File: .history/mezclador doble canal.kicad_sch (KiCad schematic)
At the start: 31 parts, among them J1 Conn_Coaxial, J2 Conn_Coaxial, J3 Conn_Coaxial, J4 Conn_Coaxial, J5 Conn_Coaxial, J6 Conn_Coaxial, J7 Screw_Terminal_01x02, U1 NE5532

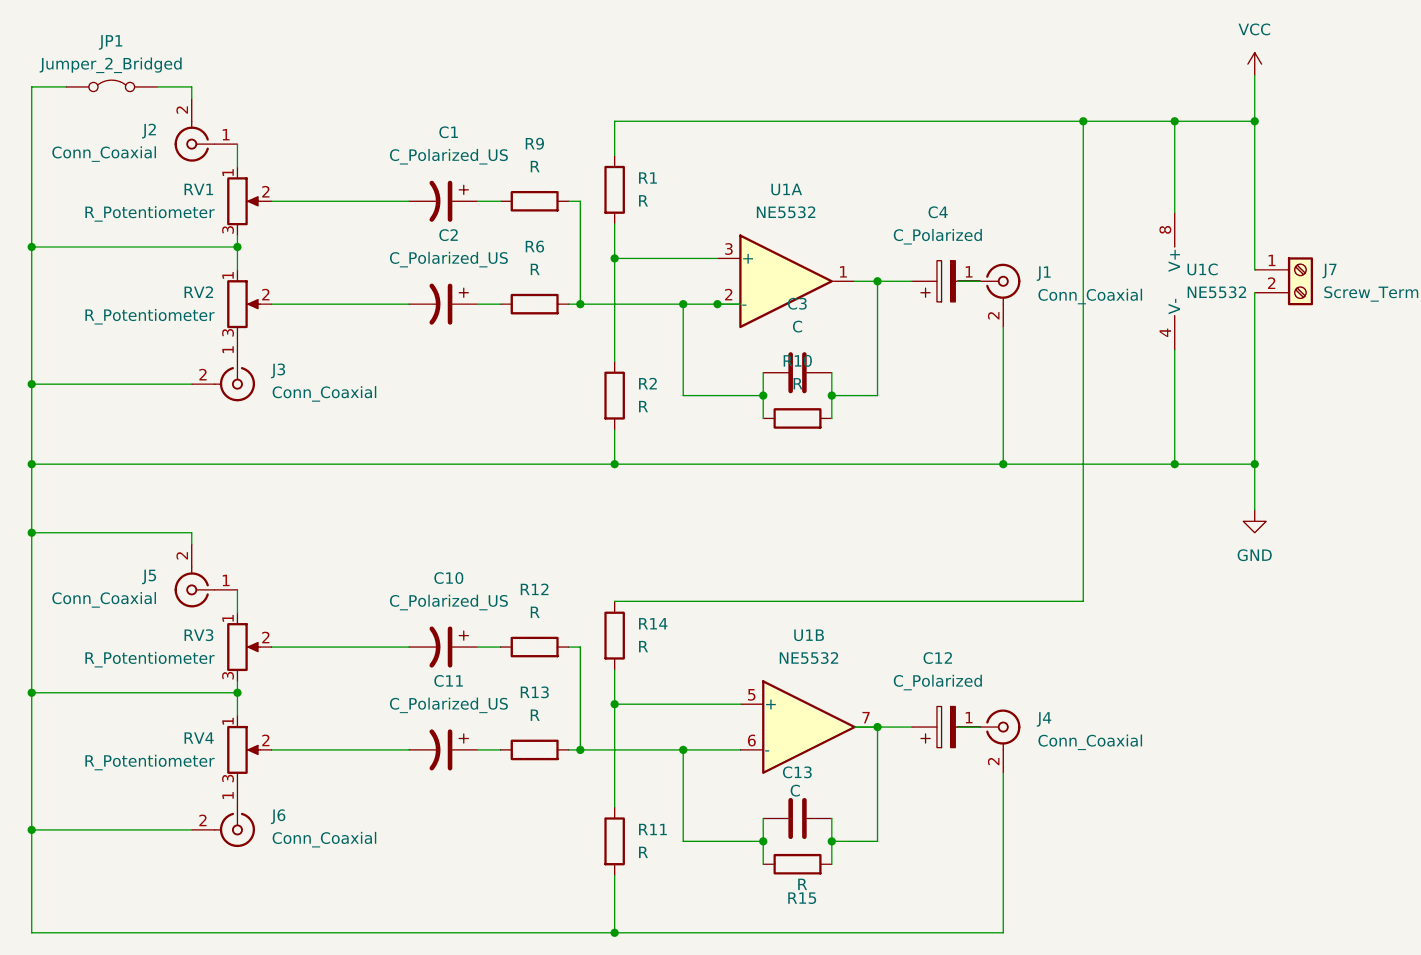
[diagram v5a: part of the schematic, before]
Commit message: mejorando distribucion de componentes
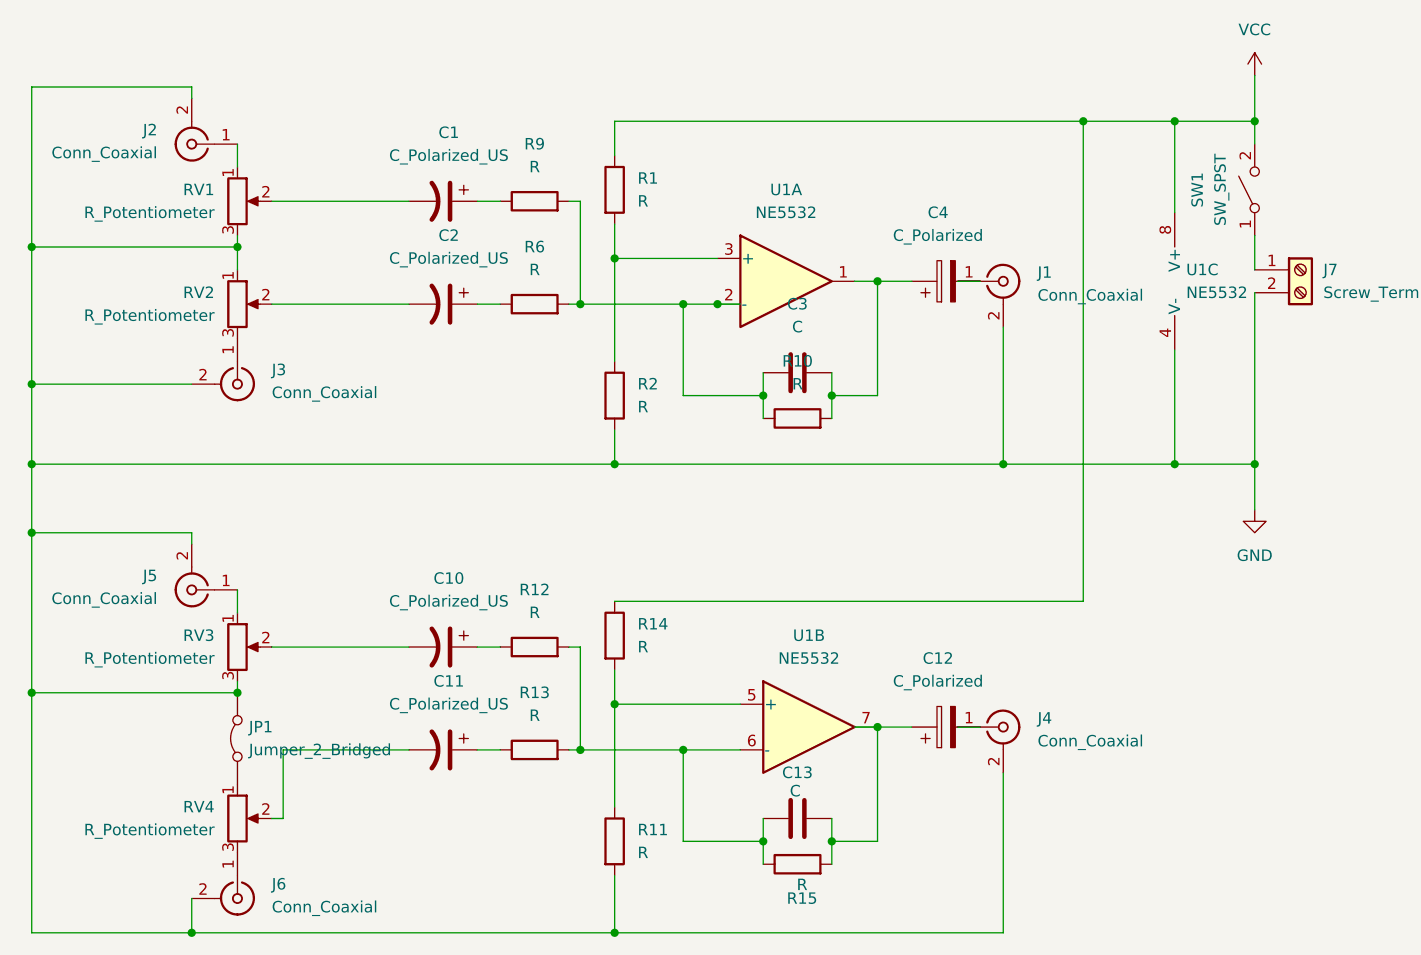
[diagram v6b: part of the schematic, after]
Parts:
- added SW1: SW_SPST, personal:double wire, symbol Switch:SW_SPST
- J4, J6: footprint Connector:JWT_A3963_1x02_P3.96mm_Vertical -> personal:double wire
- RV4: footprint Potentiometer_THT:Potentiometer_Bourns_3296W_Vertical -> personal:potentiometer pads
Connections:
- net GND: now also J2.2 (Ext), JP1.2 (B); no longer JP1.1 (A), RV4.1
- net VCC: now also SW1.2 (B); no longer J7.1 (Pin_1)
- new net: JP1.1 (A), RV4.1
- new net: J7.1 (Pin_1), SW1.1 (A)
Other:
- moved on the sheet: J6, RV4

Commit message: agregando preamplificador microfomo
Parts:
- added C5: C_Polarized_US, symbol Device:C_Polarized_US
- added J8: Conn_Coaxial, symbol Connector:Conn_Coaxial
- added R3: R, Package_LCC:PLCC-84_29.3x29.3mm_P1.27mm, symbol Device:R
- added U2: TL071, symbol Amplifier_Operational:TL071
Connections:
- new net: C5.2, J8.1 (In)
- new net: C5.1, R3.1
- new net: R3.2, U2.2 (-)

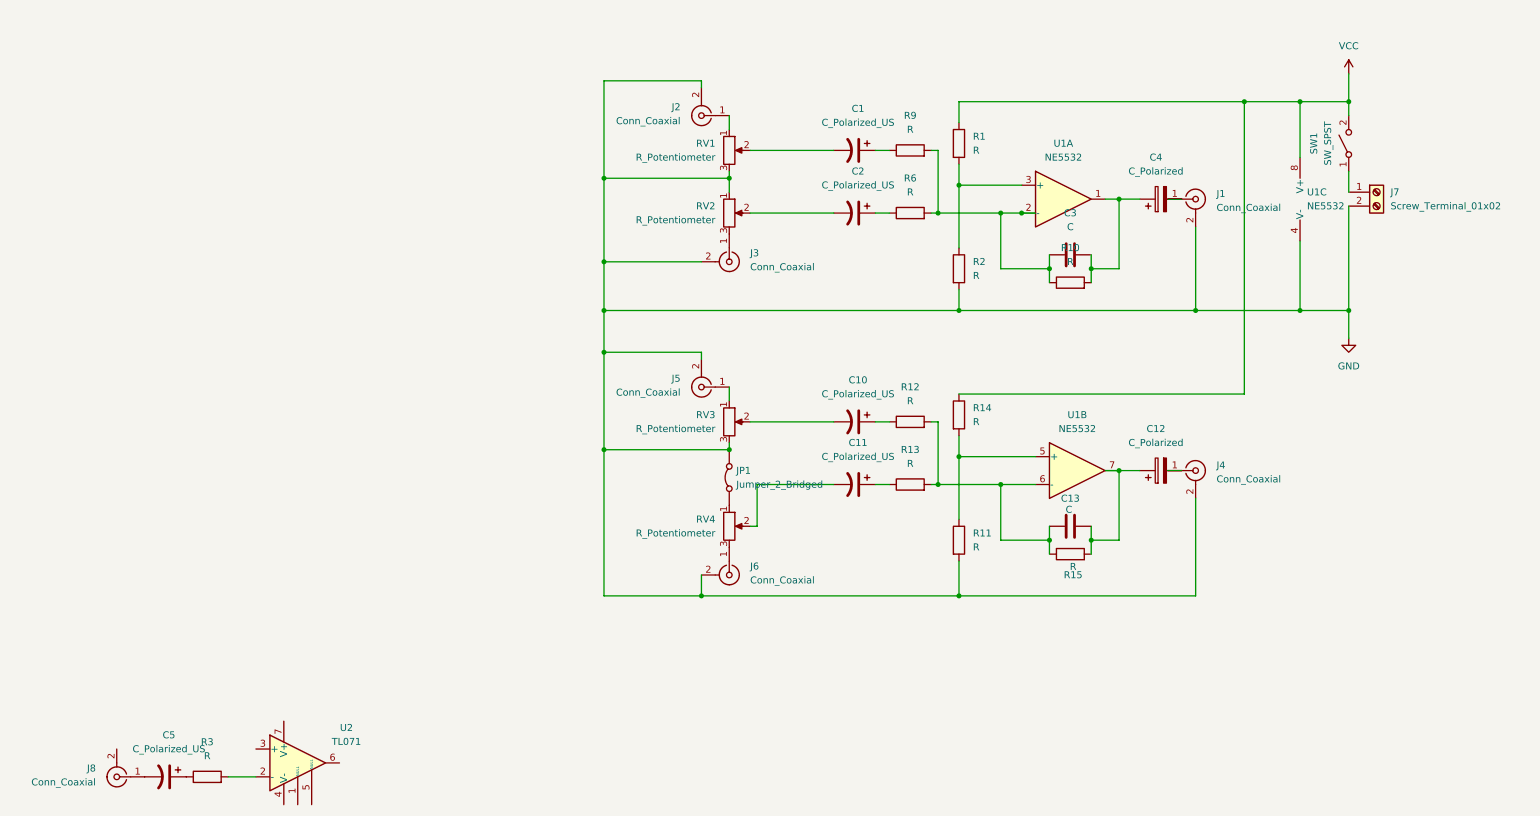
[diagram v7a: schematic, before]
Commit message: agregando preamplificador microfono
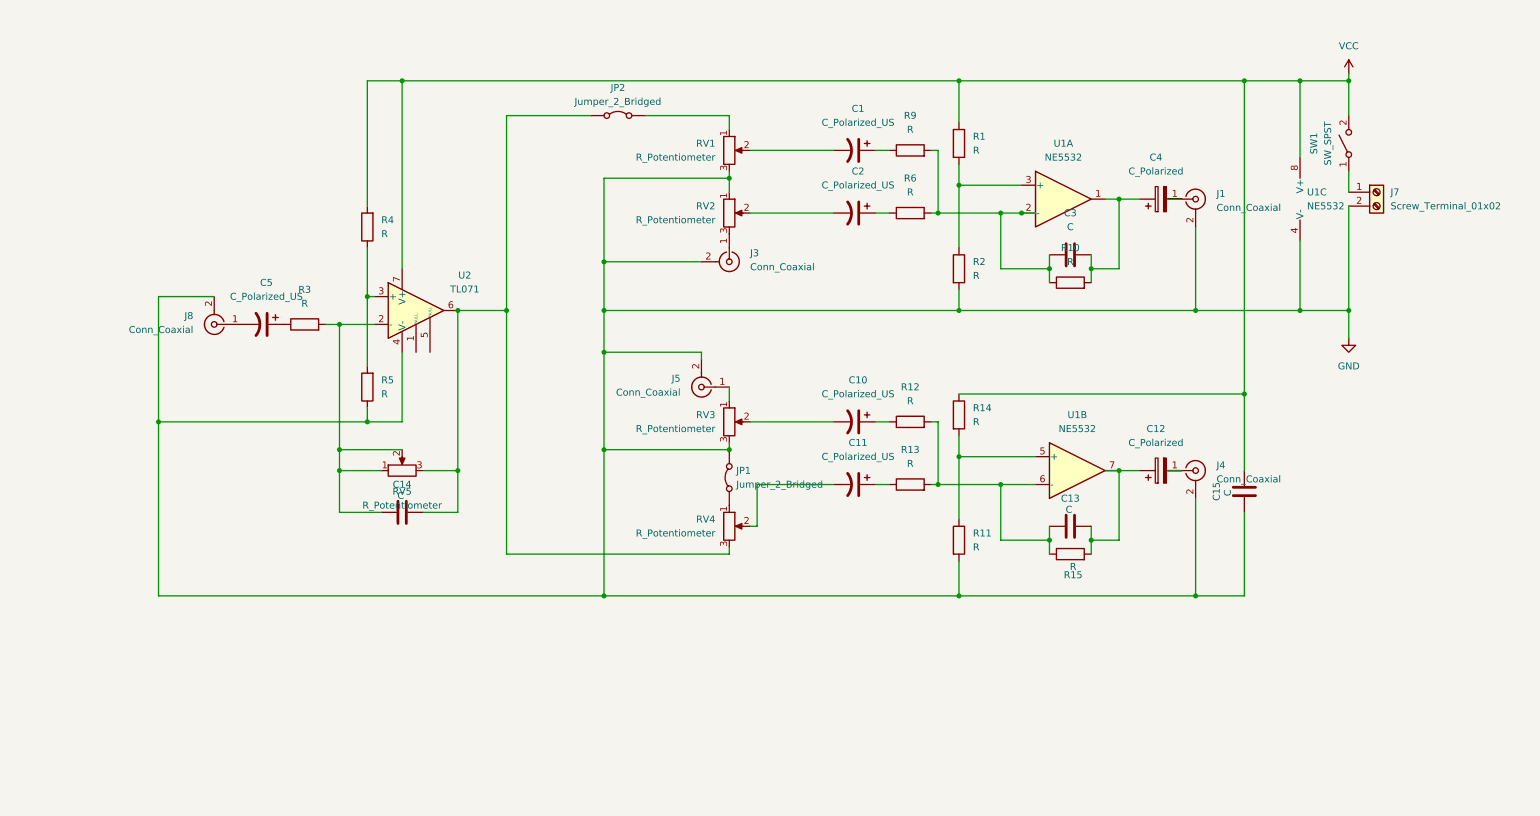
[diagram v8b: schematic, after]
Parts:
- removed J2, J6: Conn_Coaxial, personal:double wire, symbol Connector:Conn_Coaxial
- added C14, C15: C, Capacitor_THT:C_Disc_D5.0mm_W2.5mm_P5.00mm, symbol Device:C
- added JP2: Jumper_2_Bridged, personal:Jumper_Wire_10mm, symbol Jumper:Jumper_2_Bridged
- added R4, R5: R, Resistor_THT:R_Axial_DIN0207_L6.3mm_D2.5mm_P10.16mm_Horizontal, symbol Device:R
- added RV5: R_Potentiometer, personal:potentiometer pads, symbol Device:R_Potentiometer
- C5: footprint (none) -> Capacitor_THT:C_Disc_D5.0mm_W2.5mm_P5.00mm
- J8: footprint (none) -> personal:double wire
- R3: footprint Package_LCC:PLCC-84_29.3x29.3mm_P1.27mm -> Resistor_THT:R_Axial_DIN0207_L6.3mm_D2.5mm_P10.16mm_Horizontal
- U2: footprint (none) -> Package_DIP:DIP-8_W7.62mm
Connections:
- net GND: now also J8.2 (Ext), U2.4 (V-), C15.1, R5.1
- net VCC: now also U2.7 (V+), C15.2, R4.2
- net at RV4.3: now also U2.6, C14.2, JP2.1 (A), RV5.3
- net at R3.2, U2.2 (-): now also C14.1, RV5.1, RV5.2
- net at RV1.1: now also JP2.2 (B)
- net at U2.3 (+): now also R4.1, R5.2
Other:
- moved on the sheet: C5, J8, R3, U2
